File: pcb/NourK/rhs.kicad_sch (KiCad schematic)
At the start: 1 part, among them J1 SJ-435107RS

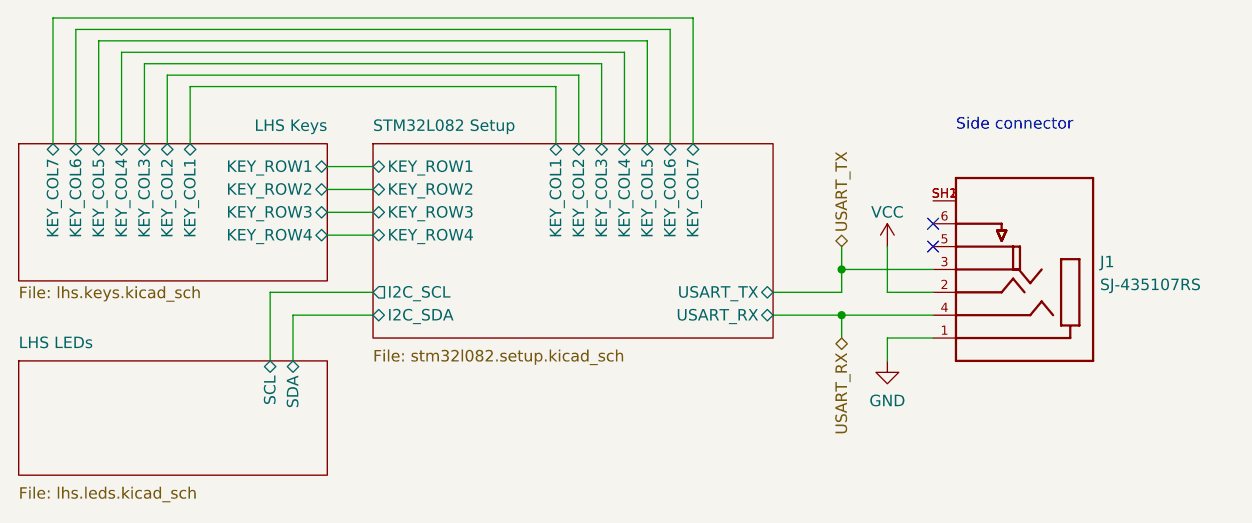
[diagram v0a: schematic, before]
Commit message: Add RHS schematics sheets
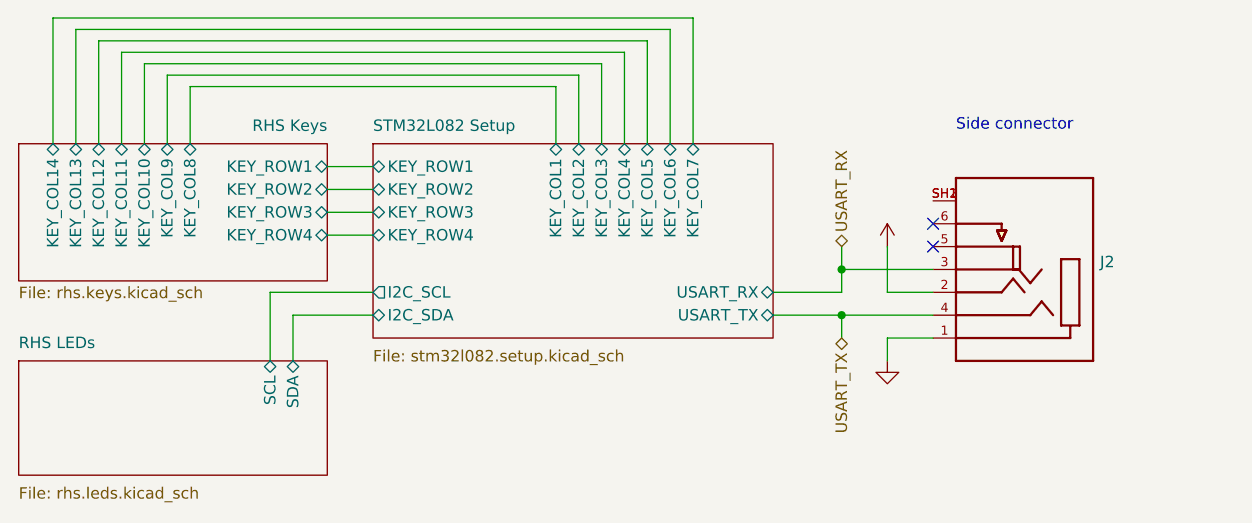
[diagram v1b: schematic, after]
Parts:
- removed J1: SJ-435107RS, Nour_KB:CUI_SJ-435107RS, symbol Nour_KB:SJ-435107RS
- added J2: (no value), symbol Nour_KB:SJ-435107RS
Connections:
- net GND: now also J2.1
- net USART_RX: now also J2.3
- net USART_TX: now also J2.4
- net VCC: now also J2.2
- new net: J2.SH1, J2.SH2
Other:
- removed sheet LHS Keys
- removed sheet LHS LEDs
- added sheet RHS Keys (rhs.keys.kicad_sch)
- added sheet RHS LEDs (rhs.leds.kicad_sch)
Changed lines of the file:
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@@
     (effects (font (size 1.27 1.27)) (justify left bottom))
   )
-  (hierarchical_label "USART_RX" (shape bidirectional) (at 173.99 82.55 270)
-    (effects (font (size 1.27 1.27)) (justify right))
-  )
-  (hierarchical_label "USART_TX" (shape bidirectional) (at 173.99 72.39 90)
+  (hierarchical_label "USART_RX" (shape bidirectional) (at 173.99 72.39 90)
     (effects (font (size 1.27 1.27)) (justify left))
   )
-  (symbol (lib_id "power:GND") (at 179.07 85.09 0) (unit 1)
-    (in_bom yes) (on_board yes) (fields_autoplaced)
-    (property "Reference" "#PWR05" (id 0) (at 179.07 91.44 0)
-      (effects (font (size 1.27 1.27)) hide)
-    )
-    (property "Value" "GND" (id 1) (at 179.07 89.5334 0))
-    (property "Footprint" "" (id 2) (at 179.07 85.09 0)
-      (effects (font (size 1.27 1.27)) hide)
-    )
-    (property "Datasheet" "" (id 3) (at 179.07 85.09 0)
-      (effects (font (size 1.27 1.27)) hide)
-    )
-    (pin "1")
-  )
-  (symbol (lib_id "power:VCC") (at 179.07 72.39 0) (unit 1)
-    (in_bom yes) (on_board yes)
-    (property "Reference" "#PWR04" (id 0) (at 179.07 76.2 0)
-      (effects (font (size 1.27 1.27)) hide)
-    )
-    (property "Value" "VCC" (id 1) (at 179.07 68.58 0))
-    (property "Footprint" "" (id 2) (at 179.07 72.39 0)
-      (effects (font (size 1.27 1.27)) hide)
-    )
-    (property "Datasheet" "" (id 3) (at 179.07 72.39 0)
-      (effects (font (size 1.27 1.27)) hide)
-    )
-    (pin "1")
+  (hierarchical_label "USART_TX" (shape bidirectional) (at 173.99 82.55 270)
+    (effects (font (size 1.27 1.27)) (justify right))
   )
   (symbol (lib_id "Nour_KB:SJ-435107RS") (at 194.31 74.93 180) (unit 1)
     (in_bom yes) (on_board yes) (fields_autoplaced)
-    (property "Reference" "J1" (id 0) (at 202.692 74.0953 0)
+    (property "Reference" "J2" (id 0) (at 202.692 74.0953 0)
       (effects (font (size 1.27 1.27)) (justify right))
     )
-    (property "Value" "SJ-435107RS" (id 1) (at 202.692 76.6322 0)
+    (property "Value" "" (id 1) (at 202.692 76.6322 0)
       (effects (font (size 1.27 1.27)) (justify right))
     )
-    (property "Footprint" "Nour_KB:CUI_SJ-435107RS" (id 2) (at 194.31 74.93 0)
+    (property "Footprint" "" (id 2) (at 194.31 74.93 0)
       (effects (font (size 1.27 1.27)) (justify left bottom) hide)
     )
@@
     (pin "SH2")
   )
+  (symbol (lib_id "power:VCC") (at 179.07 72.39 0) (unit 1)
+    (in_bom yes) (on_board yes)
+    (property "Reference" "#PWR06" (id 0) (at 179.07 76.2 0)
+      (effects (font (size 1.27 1.27)) hide)
+    )
+    (property "Value" "" (id 1) (at 179.07 68.58 0))
+    (property "Footprint" "" (id 2) (at 179.07 72.39 0)
+      (effects (font (size 1.27 1.27)) hide)
+    )
+    (property "Datasheet" "" (id 3) (at 179.07 72.39 0)
+      (effects (font (size 1.27 1.27)) hide)
+    )
+    (pin "1")
+  )
+  (symbol (lib_id "power:GND") (at 179.07 85.09 0) (unit 1)
+    (in_bom yes) (on_board yes) (fields_autoplaced)
+    (property "Reference" "#PWR07" (id 0) (at 179.07 91.44 0)
+      (effects (font (size 1.27 1.27)) hide)
+    )
+    (property "Value" "" (id 1) (at 179.07 89.5334 0))
+    (property "Footprint" "" (id 2) (at 179.07 85.09 0)
+      (effects (font (size 1.27 1.27)) hide)
+    )
+    (property "Datasheet" "" (id 3) (at 179.07 85.09 0)
+      (effects (font (size 1.27 1.27)) hide)
+    )
+    (pin "1")
+  )
   (sheet (at 82.55 85.09) (size 34.29 12.7)
     (stroke (width 0.1524) (type solid) (color 0 0 0 0))
     (fill (color 0 0 0 0.0000))
-    (property "Sheet name" "LHS LEDs" (id 0) (at 82.55 83.82 0)
+    (property "Sheet name" "RHS LEDs" (id 0) (at 82.55 83.82 0)
       (effects (font (size 1.27 1.27)) (justify left bottom))
     )
-    (property "Sheet file" "lhs.leds.kicad_sch" (id 1) (at 82.55 99.06 0)
+    (property "Sheet file" "rhs.leds.kicad_sch" (id 1) (at 82.55 99.06 0)
       (effects (font (size 1.27 1.27)) (justify left top))
     )
@@
       (effects (font (size 1.27 1.27)) (justify left top))
     )
-    (pin "USART_TX" bidirectional (at 166.37 77.47 0)
+    (pin "USART_TX" bidirectional (at 166.37 80.01 0)
       (effects (font (size 1.27 1.27)) (justify right))
     )
-    (pin "USART_RX" bidirectional (at 166.37 80.01 0)
+    (pin "USART_RX" bidirectional (at 166.37 77.47 0)
       (effects (font (size 1.27 1.27)) (justify right))
     )
@@
     (stroke (width 0.1524) (type solid) (color 0 0 0 0))
     (fill (color 0 0 0 0.0000))
-    (property "Sheet name" "LHS Keys" (id 0) (at 116.84 59.69 0)
+    (property "Sheet name" "RHS Keys" (id 0) (at 116.84 59.69 0)
       (effects (font (size 1.27 1.27)) (justify right bottom))
     )
-    (property "Sheet file" "lhs.keys.kicad_sch" (id 1) (at 82.55 76.7846 0)
+    (property "Sheet file" "rhs.keys.kicad_sch" (id 1) (at 82.55 76.7846 0)
       (effects (font (size 1.27 1.27)) (justify left top))
     )
@@
       (effects (font (size 1.27 1.27)) (justify right))
     )
-    (pin "KEY_COL1" bidirectional (at 101.6 60.96 90)
-      (effects (font (size 1.27 1.27)) (justify right))
-    )
     (pin "KEY_ROW2" bidirectional (at 116.84 66.04 0)
       (effects (font (size 1.27 1.27)) (justify right))
@@
       (effects (font (size 1.27 1.27)) (justify right))
     )
-    (pin "KEY_COL3" bidirectional (at 96.52 60.96 90)
+    (pin "KEY_COL13" bidirectional (at 88.9 60.96 90)
       (effects (font (size 1.27 1.27)) (justify right))
     )
-    (pin "KEY_COL4" bidirectional (at 93.98 60.96 90)
+    (pin "KEY_COL14" bidirectional (at 86.36 60.96 90)
       (effects (font (size 1.27 1.27)) (justify right))
     )
-    (pin "KEY_COL6" bidirectional (at 88.9 60.96 90)
+    (pin "KEY_COL12" bidirectional (at 91.44 60.96 90)
       (effects (font (size 1.27 1.27)) (justify right))
     )
-    (pin "KEY_COL5" bidirectional (at 91.44 60.96 90)
+    (pin "KEY_COL9" bidirectional (at 99.06 60.96 90)
       (effects (font (size 1.27 1.27)) (justify right))
     )
-    (pin "KEY_COL2" bidirectional (at 99.06 60.96 90)
+    (pin "KEY_COL10" bidirectional (at 96.52 60.96 90)
       (effects (font (size 1.27 1.27)) (justify right))
     )
-    (pin "KEY_COL7" bidirectional (at 86.36 60.96 90)
+    (pin "KEY_COL8" bidirectional (at 101.6 60.96 90)
       (effects (font (size 1.27 1.27)) (justify right))
     )
+    (pin "KEY_COL11" bidirectional (at 93.98 60.96 90)
+      (effects (font (size 1.27 1.27)) (justify right))
+    )

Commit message: Draft LHS tracks
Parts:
- removed J2: (no value), symbol Nour_KB:SJ-435107RS
- added J4: SJ-435107RS, Nour_KB:CUI_SJ-435107RS, symbol Nour_KB:SJ-435107RS
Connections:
- net GND: now also J4.1, J4.SH1, J4.SH2
- net VCC: now also J4.2
- new net USART.RX: J4.4
- new net USART.TX: J4.3
- no-connect marks 2 -> 3
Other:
- removed sheet STM32L082 Setup
- added sheet RHS Core (core.kicad_sch)
- sheet RHS Keys ports: added KEY{ROW[1..10] COL[1..10]}; removed KEY_COL10, KEY_COL11, KEY_COL12, KEY_COL13, KEY_COL14, KEY_COL8, KEY_COL9, KEY_ROW1, KEY_ROW2, KEY_ROW3, KEY_ROW4
- sheet RHS LEDs ports: added LED{CS_COL[1..16]}, LED{SW_RED[1..4] SW_GREEN[1..4] SW_BLUE[1..4]}; removed SCL, SDA
- note added: "B2B connector"
- note removed: "Side connector"

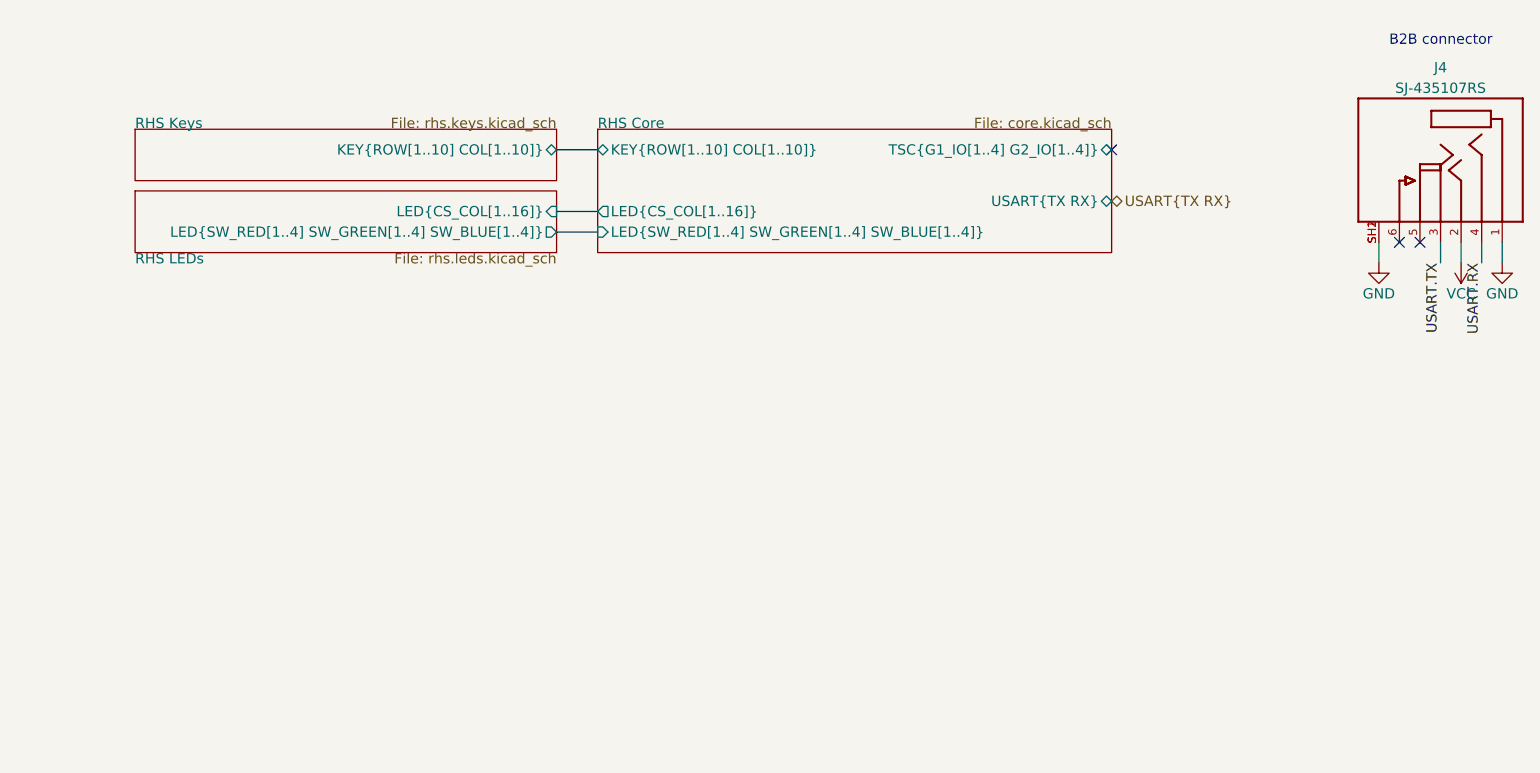
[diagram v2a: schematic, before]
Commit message: Re-traced RHS
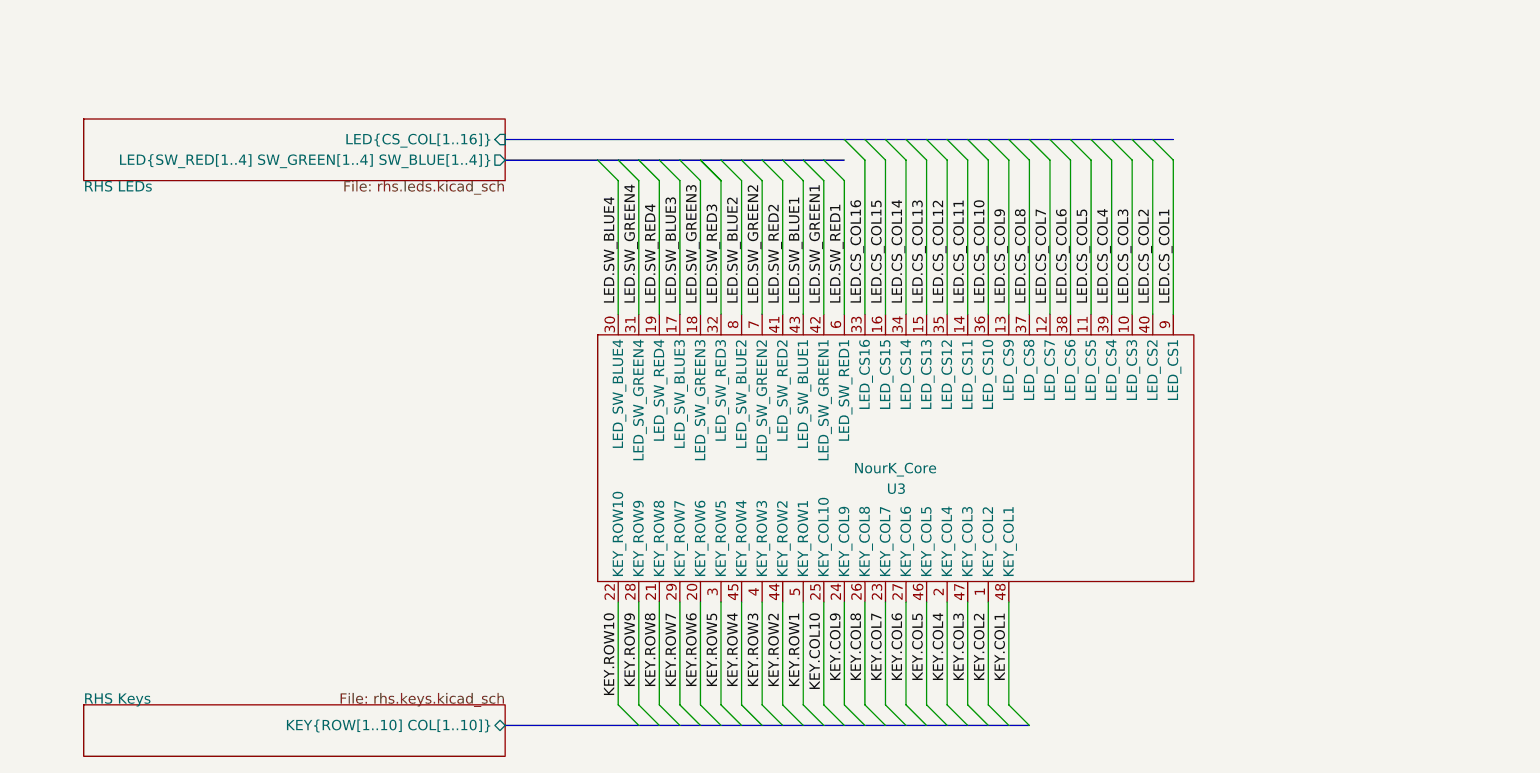
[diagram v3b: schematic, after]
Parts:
- removed J4: SJ-435107RS, Nour_KB:CUI_SJ-435107RS, symbol Nour_KB:SJ-435107RS
- added U3: NourK_Core, Nour_KB:NourKB_Core_2, symbol Nour_KB:NourK_Core_3
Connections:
- new net KEY.COL1: U3.48 (KEY_COL1)
- new net KEY.COL10: U3.25 (KEY_COL10)
- new net KEY.COL2: U3.1 (KEY_COL2)
- new net KEY.COL3: U3.47 (KEY_COL3)
- new net KEY.COL4: U3.2 (KEY_COL4)
- new net KEY.COL5: U3.46 (KEY_COL5)
- new net KEY.COL6: U3.27 (KEY_COL6)
- new net KEY.COL7: U3.23 (KEY_COL7)
- new net KEY.COL8: U3.26 (KEY_COL8)
- new net KEY.COL9: U3.24 (KEY_COL9)
- new net KEY.ROW1: U3.5 (KEY_ROW1)
- new net KEY.ROW10: U3.22 (KEY_ROW10)
- new net KEY.ROW2: U3.44 (KEY_ROW2)
- new net KEY.ROW3: U3.4 (KEY_ROW3)
- new net KEY.ROW4: U3.45 (KEY_ROW4)
- new net KEY.ROW5: U3.3 (KEY_ROW5)
- new net KEY.ROW6: U3.20 (KEY_ROW6)
- new net KEY.ROW7: U3.29 (KEY_ROW7)
- new net KEY.ROW8: U3.21 (KEY_ROW8)
- new net KEY.ROW9: U3.28 (KEY_ROW9)
- new net LED.CS_COL1: U3.9 (LED_CS1)
- new net LED.CS_COL10: U3.36 (LED_CS10)
- new net LED.CS_COL11: U3.14 (LED_CS11)
- new net LED.CS_COL12: U3.35 (LED_CS12)
- new net LED.CS_COL13: U3.15 (LED_CS13)
- new net LED.CS_COL14: U3.34 (LED_CS14)
- new net LED.CS_COL15: U3.16 (LED_CS15)
- new net LED.CS_COL16: U3.33 (LED_CS16)
- new net LED.CS_COL2: U3.40 (LED_CS2)
- new net LED.CS_COL3: U3.10 (LED_CS3)
- new net LED.CS_COL4: U3.39 (LED_CS4)
- new net LED.CS_COL5: U3.11 (LED_CS5)
- new net LED.CS_COL6: U3.38 (LED_CS6)
- new net LED.CS_COL7: U3.12 (LED_CS7)
- new net LED.CS_COL8: U3.37 (LED_CS8)
- new net LED.CS_COL9: U3.13 (LED_CS9)
- new net LED.SW_BLUE1: U3.43 (LED_SW_BLUE1)
- new net LED.SW_BLUE2: U3.8 (LED_SW_BLUE2)
- new net LED.SW_BLUE3: U3.17 (LED_SW_BLUE3)
- new net LED.SW_BLUE4: U3.30 (LED_SW_BLUE4)
- new net LED.SW_GREEN1: U3.42 (LED_SW_GREEN1)
- new net LED.SW_GREEN2: U3.7 (LED_SW_GREEN2)
- new net LED.SW_GREEN3: U3.18 (LED_SW_GREEN3)
- new net LED.SW_GREEN4: U3.31 (LED_SW_GREEN4)
- new net LED.SW_RED1: U3.6 (LED_SW_RED1)
- new net LED.SW_RED2: U3.41 (LED_SW_RED2)
- new net LED.SW_RED3: U3.32 (LED_SW_RED3)
- new net LED.SW_RED4: U3.19 (LED_SW_RED4)
- no-connect marks 3 -> 0
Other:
- removed sheet RHS Core
- note removed: "B2B connector"
